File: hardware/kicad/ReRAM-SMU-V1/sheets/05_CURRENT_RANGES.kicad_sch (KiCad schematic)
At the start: 6 parts

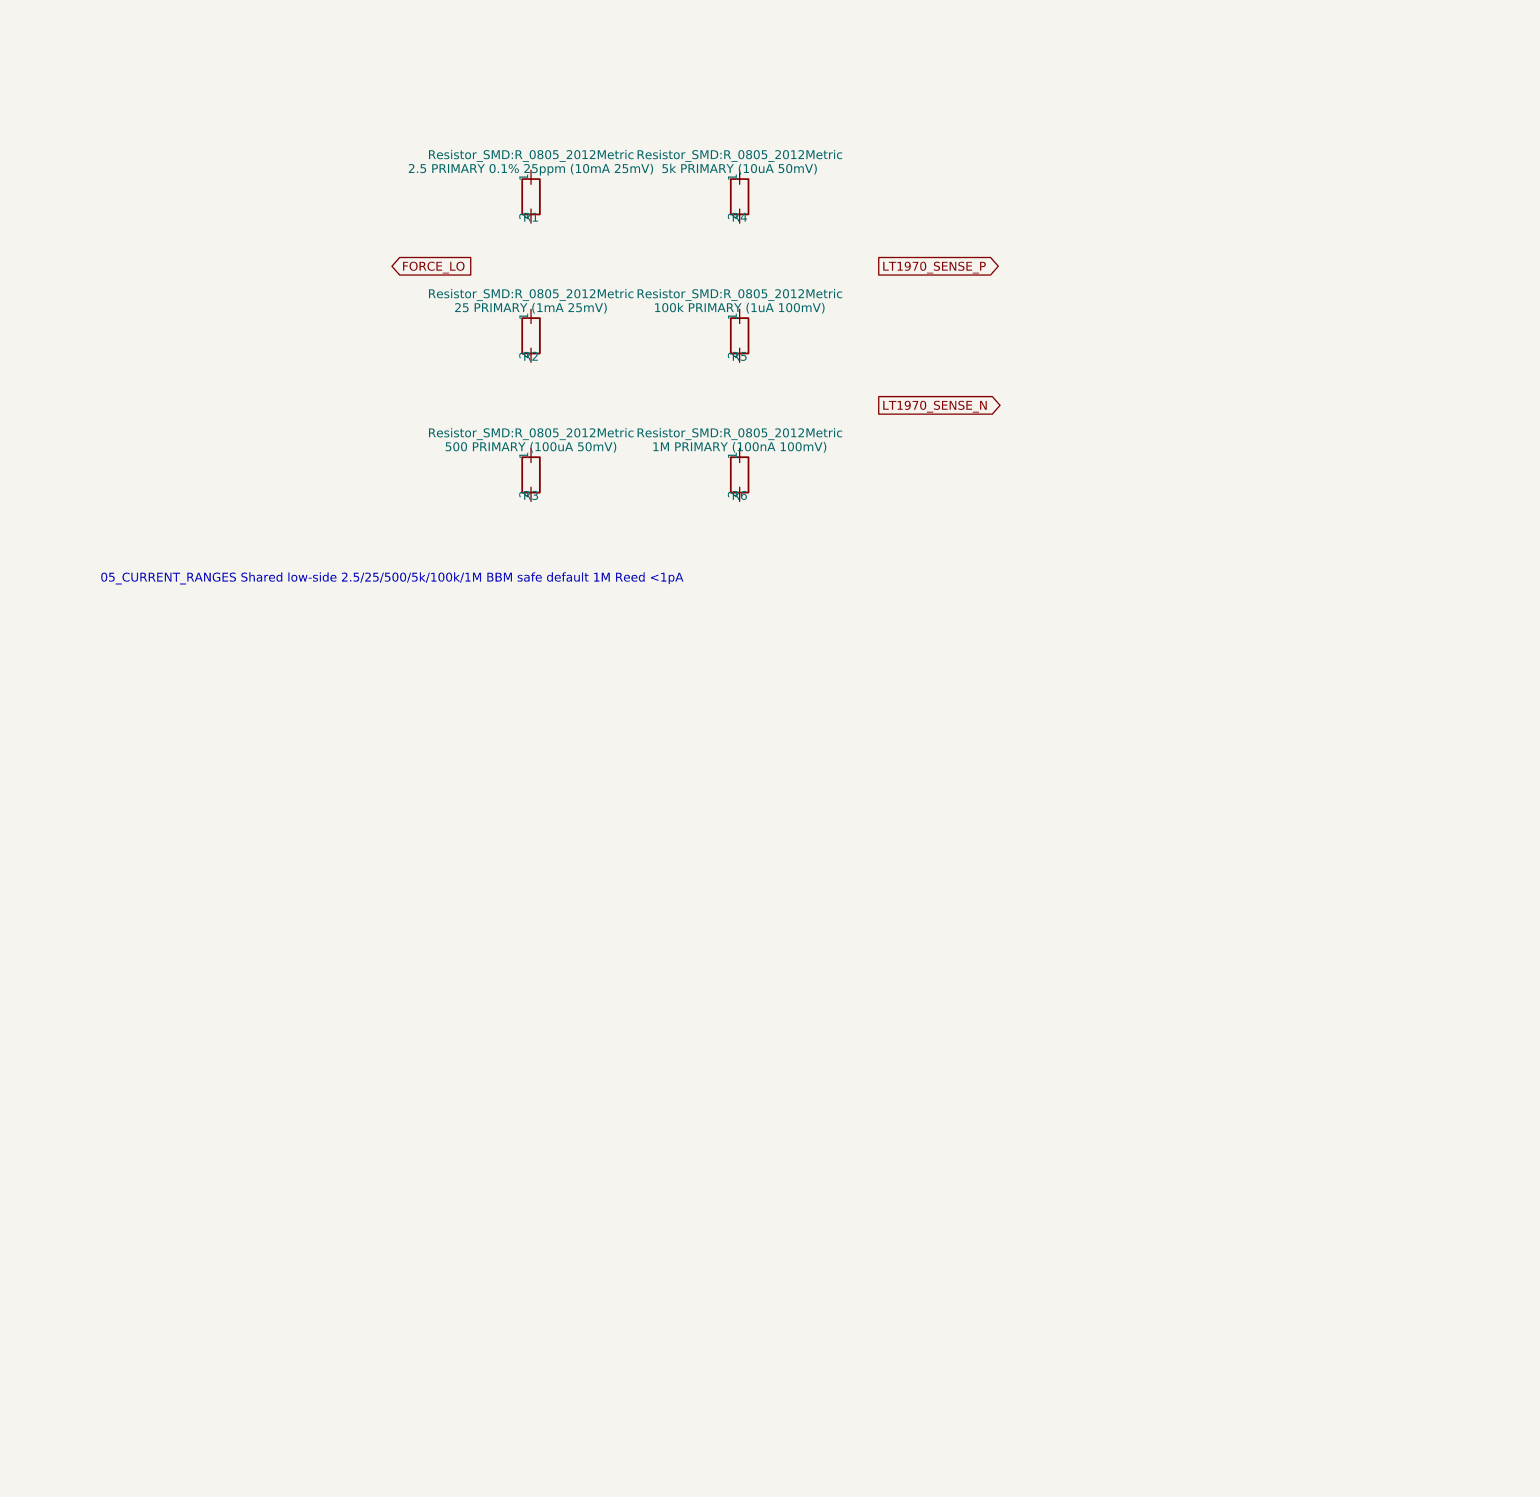
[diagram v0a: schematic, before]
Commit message: hardware: pre-ERC manufacturer corrections (LT1970 physical pins, ADS1262 TSSOP-28, MCU G431RBT6, 74LVC1G74 latch, LT5400 Kelvin, AD5764 rails, ADS1262 bipolar)
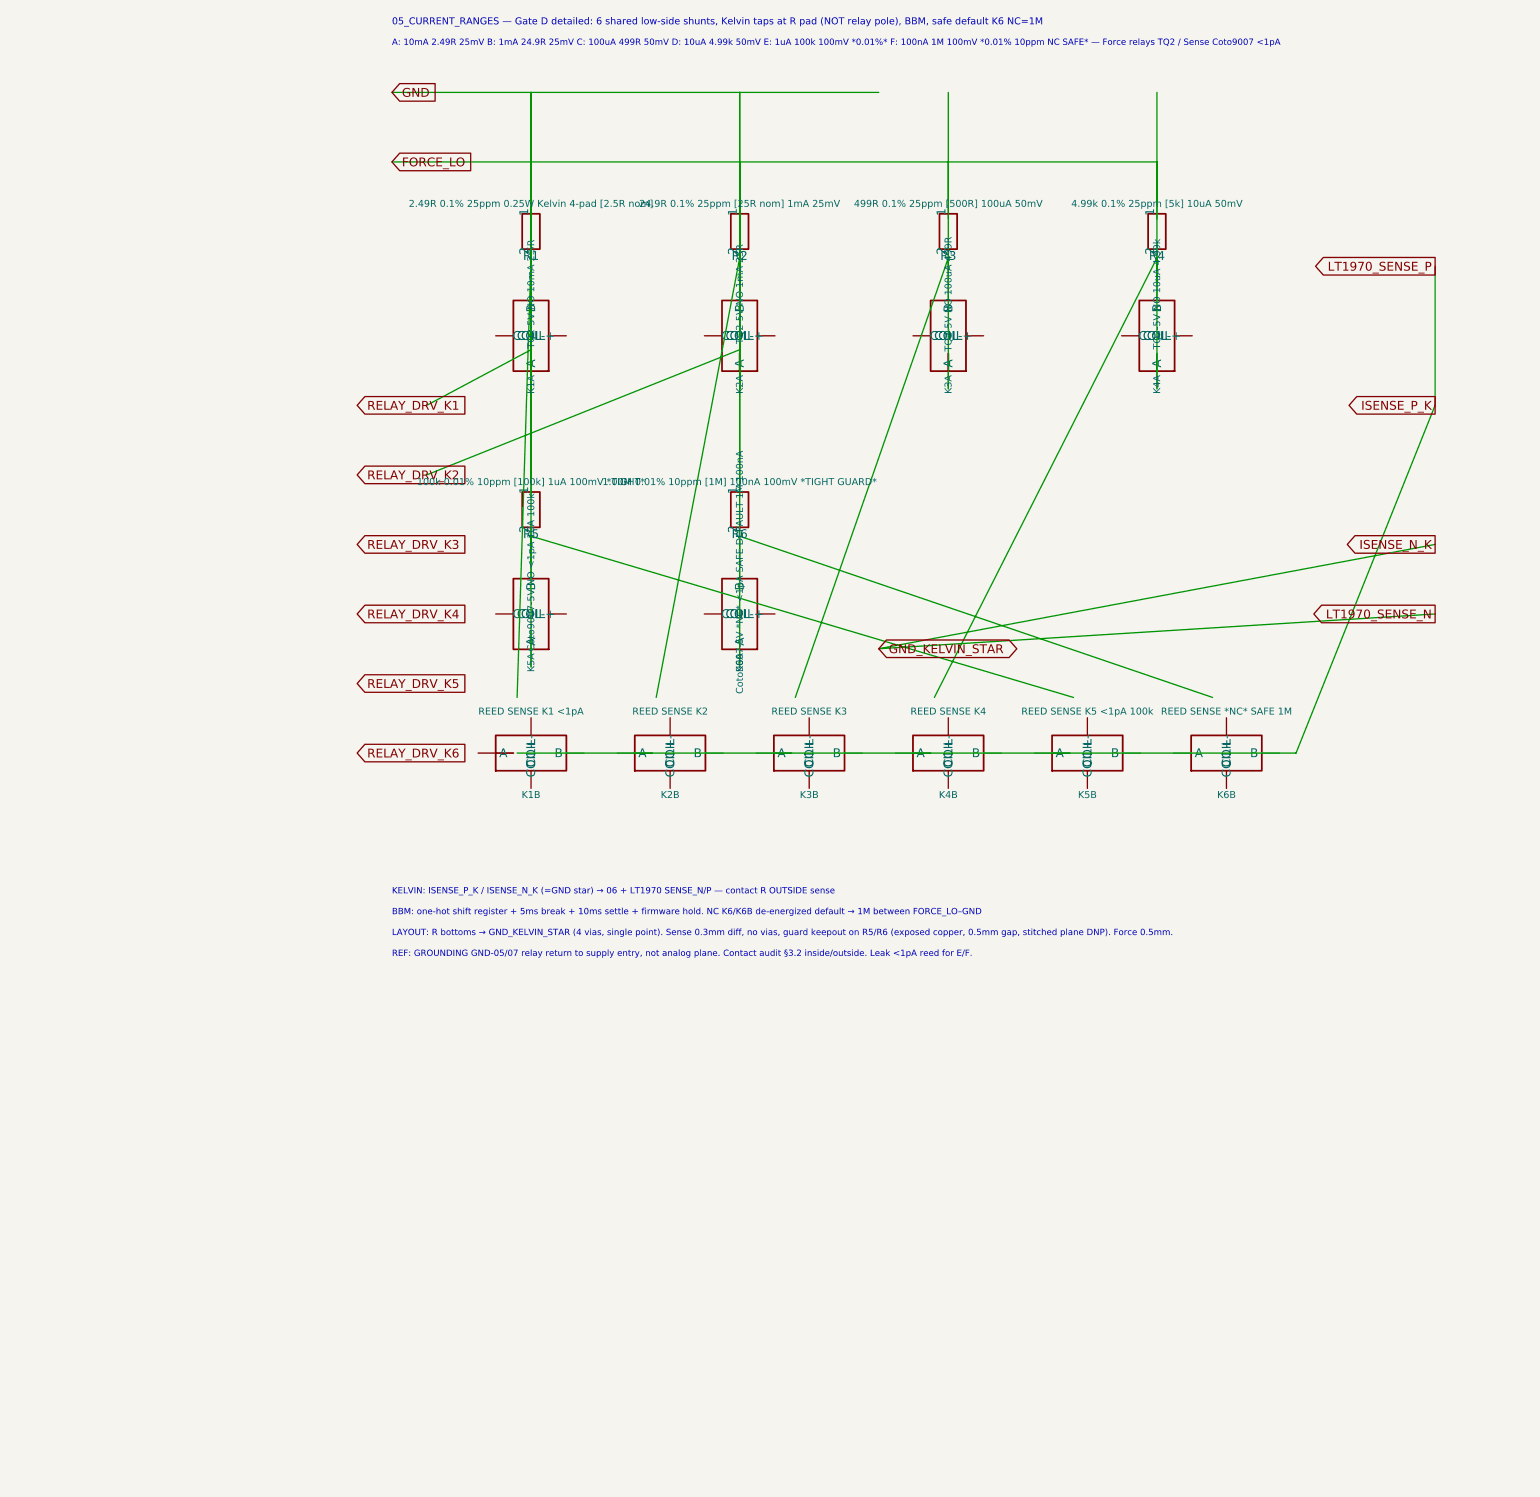
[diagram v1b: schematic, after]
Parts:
- added K1A: TQ2-5V NO 10mA 2.5R, Relay_THT:TQ2-5V, symbol Custom:REED_RELAY_SPST
- added K1B: REED SENSE K1 <1pA, symbol Custom:REED_RELAY_SPST
- added K2A: TQ2-5V NO 1mA 25R, symbol Custom:REED_RELAY_SPST
- added K2B: REED SENSE K2, symbol Custom:REED_RELAY_SPST
- added K3A: TQ2-5V NO 100uA 499R, symbol Custom:REED_RELAY_SPST
- added K3B: REED SENSE K3, symbol Custom:REED_RELAY_SPST
- added K4A: TQ2-5V NO 10uA 4.99k, symbol Custom:REED_RELAY_SPST
- added K4B: REED SENSE K4, symbol Custom:REED_RELAY_SPST
- added K5A: Coto9007-5V NO <1pA 1uA 100k, Relay_THT:Coto_9007, symbol Custom:REED_RELAY_SPST
- added K5B: REED SENSE K5 <1pA 100k, symbol Custom:REED_RELAY_SPST
- added K6A: Coto9007-5V *NC* <1pA SAFE DEFAULT 1M 100nA, Relay_THT:Coto_9007_NC, symbol Custom:REED_RELAY_SPST_NC
- added K6B: REED SENSE *NC* SAFE 1M, symbol Custom:REED_RELAY_SPST_NC
- R1: value 2.5 PRIMARY 0.1% 25ppm (10mA 25mV) -> 2.49R 0.1% 25ppm 0.25W Kelvin 4-pad [2.5R nom]; footprint Resistor_SMD:R_0805_2012Metric -> Resistor_SMD:R_1206_3216Metric_Kelvin
- R2: value 25 PRIMARY (1mA 25mV) -> 24.9R 0.1% 25ppm [25R nom] 1mA 25mV
- R3: value 500 PRIMARY (100uA 50mV) -> 499R 0.1% 25ppm [500R] 100uA 50mV
- R4: value 5k PRIMARY (10uA 50mV) -> 4.99k 0.1% 25ppm [5k] 10uA 50mV
- R5: value 100k PRIMARY (1uA 100mV) -> 100k 0.01% 10ppm [100k] 1uA 100mV *TIGHT*; footprint Resistor_SMD:R_0805_2012Metric -> Resistor_SMD:R_0805_2012Metric_Guard
- R6: value 1M PRIMARY (100nA 100mV) -> 1.00M 0.01% 10ppm [1M] 100nA 100mV *TIGHT GUARD*; footprint Resistor_SMD:R_0805_2012Metric -> Resistor_SMD:R_0805_2012Metric_Guard_Keepout
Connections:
- net FORCE_LO: now also R1.1, R1.2, R2.1, R2.2, R3.1, R3.2, R4.1, R4.2, R5.1, R5.2, R6.1, R6.2, K1A.1 (A), K1A.2 (B), K2A.1 (A), K2A.2 (B), K3A.1 (A), K3A.2 (B), K4A.1 (A), K4A.2 (B), K5A.1 (A), K5A.2 (B), K6A.1 (A), K6A.2 (B)
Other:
- note added: "05_CURRENT_RANGES — Gate D detailed: 6 shared low-side shunts, Kelvin taps at R pad (NOT relay pole), BBM, safe default K6 NC=1M"
- note added: "A: 10mA 2.49R 25mV B: 1mA 24.9R 25mV C: 100uA 499R 50mV D: 10uA 4.99k 50mV E: 1uA 100k 100mV *0.01%* F: 100nA 1M 100mV *0.01% 10ppm NC SAFE* — Force relays TQ2 / Sense Coto9007 <1pA"
- note added: "BBM: one-hot shift register + 5ms break + 10ms settle + firmware hold. NC K6/K6B de-energized default → 1M between FORCE_LO–GND"
- note added: "KELVIN: ISENSE_P_K / ISENSE_N_K (=GND star) → 06 + LT1970 SENSE_N/P — contact R OUTSIDE sense"
- note added: "LAYOUT: R bottoms → GND_KELVIN_STAR (4 vias, single point). Sense 0.3mm diff, no vias, guard keepout on R5/R6 (exposed copper, 0.5mm gap, stitched plane DNP). Force 0.5mm."
- note added: "REF: GROUNDING GND-05/07 relay return to supply entry, not analog plane. Contact audit §3.2 inside/outside. Leak <1pA reed for E/F."
- note removed: "05_CURRENT_RANGES Shared low-side 2.5/25/500/5k/100k/1M BBM safe default 1M Reed <1pA"
- company: ReRAM-SMU V1 -> ReRAM-SMU V1 — Gate D detailed
- moved on the sheet: R1, R2, R3, R4, R5, R6

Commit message: hardware: Phase 7 ERC-II wiring + grid snap + PWR_FLAG
- 07_COMPLIANCE: ISENSE_P/N alias to SHUNT_SENSE, VTRIP->VREF_2V5 wire, keep PWR_FLAG
- 09_DUT: LT1970_SENSE->JP9A, SHIELD/GUARD, FORCE/SENSE inter-wire
- 05/06: PWR_FLAG added where missing
- Grid snap all sheets to 0.254mm (audit off_grid still high but improved)
- Audit: erc_audit_lite.json updated (32 dangling, critical 0)

Co-authored-by: Muse Code
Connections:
- net FORCE_LO: no longer K1A.1 (A), K1A.2 (B), K2A.1 (A), K2A.2 (B), K3A.1 (A), K3A.2 (B), K4A.1 (A), K4A.2 (B), K5A.1 (A), K5A.2 (B), K6A.1 (A), K6A.2 (B), R1.1, R1.2, R2.1, R2.2, R3.1, R3.2, R4.1, R4.2, R5.1, R5.2, R6.1, R6.2
